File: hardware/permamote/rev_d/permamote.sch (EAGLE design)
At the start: 125 parts, among them J1 TC2030-JLINK-NL, J5 MICRO_USB_B_HIROSE_ZX62R-B-5P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, Q1 PMDXB950UPEL, Q10 PMDXB950UPEL, Q2 PMDXB950UPEL, Q3 PMDXB950UPEL, Q4 PMDXB950UPEL, Q5 PMDXB950UPEL, Q6 PMDXB950UPEL, Q7 PMDXB950UPEL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

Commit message: Fix exti in rev d
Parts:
- removed C21: 0.1uF, passives:CAPACITOR0402_CAP
- removed J5: MICRO_USB_B_HIROSE_ZX62R-B-5P(30), connector:MICRO_USB_B_HIROSE_ZX62R-B-5P(30)
- removed SJ2, SJ3, SJ4, SJ5: SOLDERJUMPERNC2, SparkFun-Passives:SOLDERJUMPERNC2
- removed U4: FT232RQ, ftdichip:FT232RQ
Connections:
- removed net !FTDI_RESET: SJ3.2, U4.!RESET
- removed net D+: J5.D+, U4.USBDP
- removed net D-: J5.D-, U4.USBDM
- removed net FTDI_VCCIO: SJ2.2, U4.VCCIO
- removed net N$13: C21.1, U4.3V3OUT
- removed net RXD: SJ4.1, U4.RXD
- removed net TXD: SJ5.1, U4.TXD
- removed net USB_5V: J5.+5V, U4.VCC
- net !RST: no longer SJ3.1
- net DBG_RX: no longer SJ5.2
- net DBG_TX: no longer SJ4.2
- net GND: now also U1.EXTI; no longer C21.2, J5.GND, U4.GND, U4.GND@1, U4.GND@2, U4.GND@A, U4.TEST
- net VCC: no longer SJ2.1

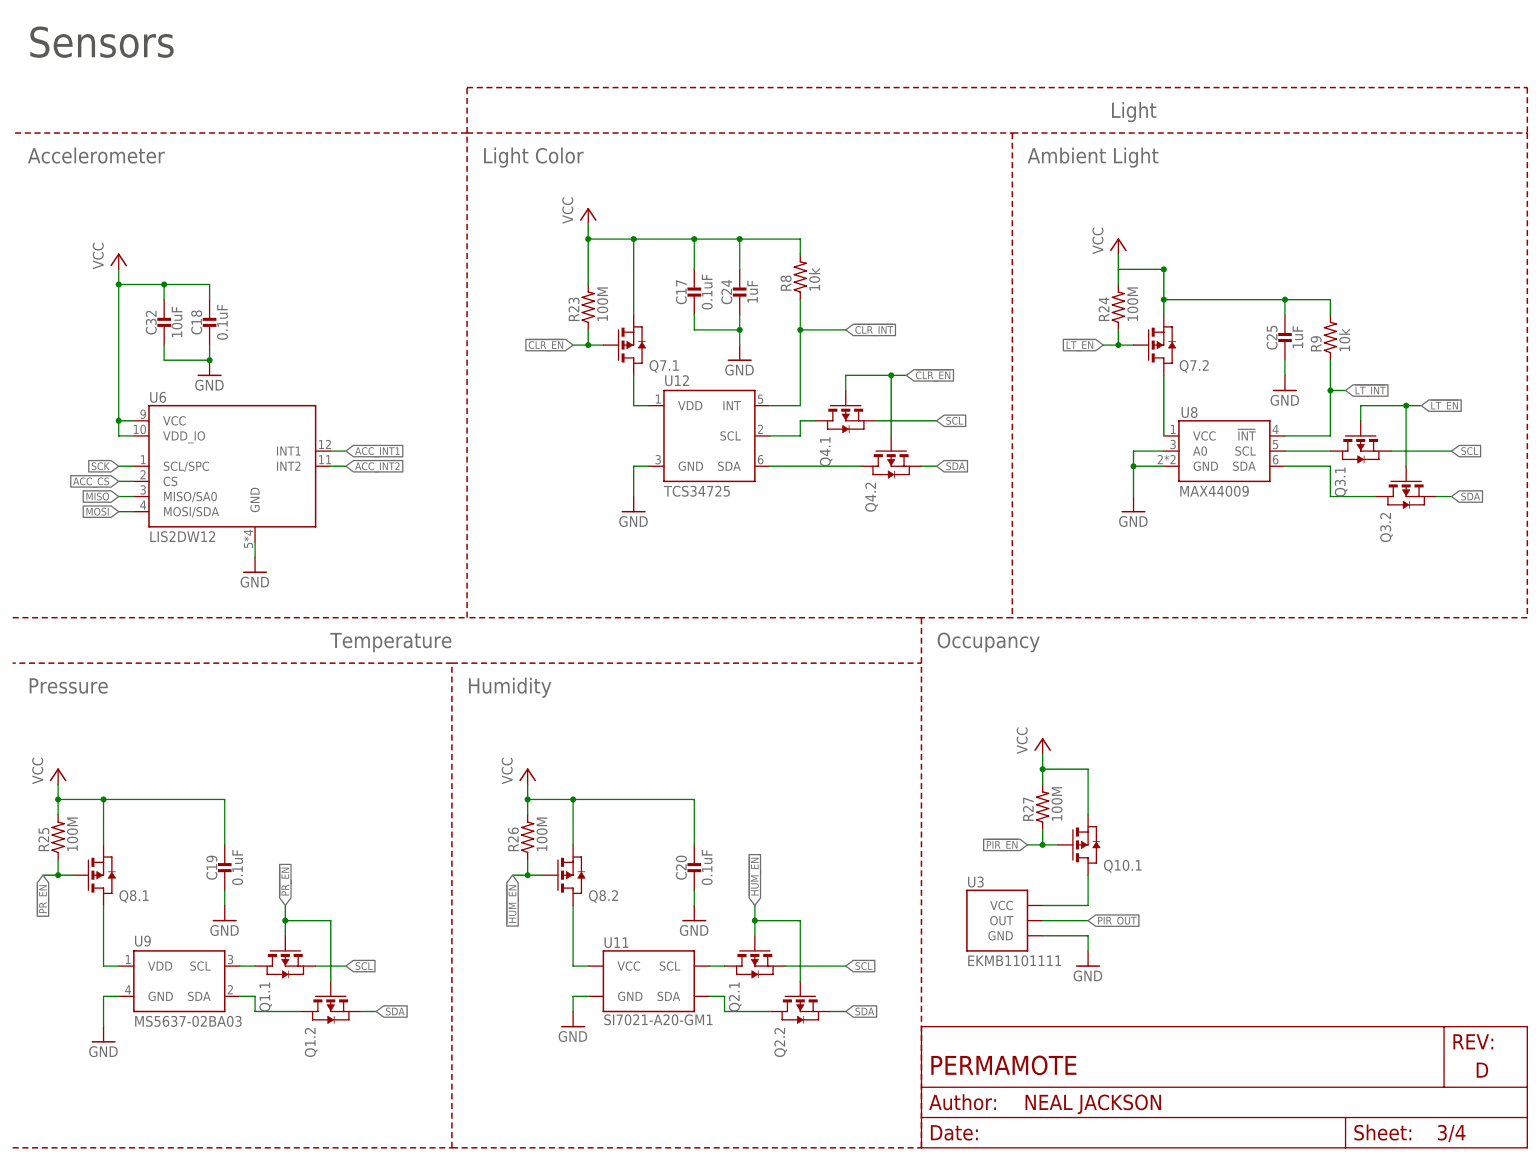
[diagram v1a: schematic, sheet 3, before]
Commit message: switch to larger coin cell, new light sensor
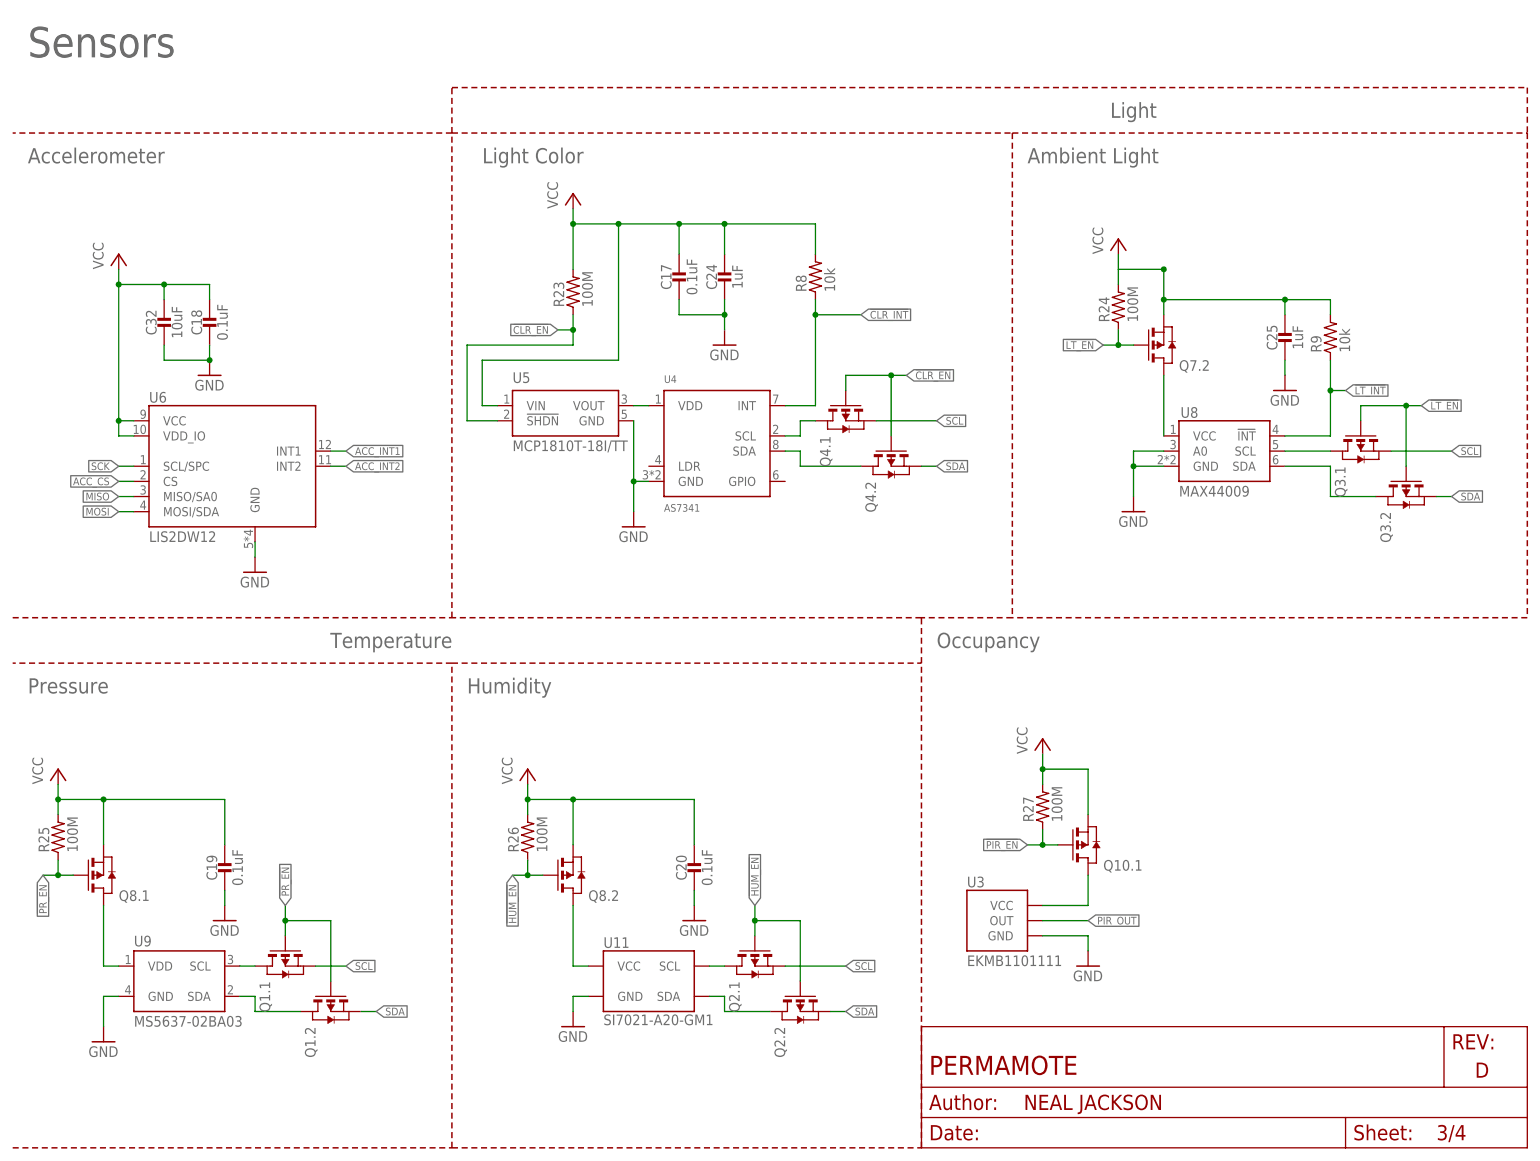
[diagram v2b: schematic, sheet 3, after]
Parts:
- removed BT2, BT3: BAT-HLD-002-THM, batteries:BAT-HLD-002-THM
- removed BT4: BAT_PACKCR123A, batteries:BAT_PACKCR123A
- removed U12: TCS34725, chips:TCS34725
- added BAT1: 2477THMCOINCELLCLIP, batteries:2477THMCOINCELLCLIP
- added U4: AS7341, chips:AS7341
- added U5: MCP1810T-18I/TT, chips:MCP1810T-18I/TT
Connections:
- removed net N$54: Q4.2.D, U12.SDA
- new net N$13: Q4.2.D, U4.SDA
- net !CLR_EN: now also U5.!SHDN; no longer Q7.1.G
- net !CLR_INT: now also U4.INT; no longer U12.INT
- net GND: now also BAT1.-, U4.GND, U5.GND; no longer BT2.-, BT3.-, BT4.-, U12.GND
- net N$31: now also U4.VDD, U5.VOUT; no longer Q7.1.D, U12.VDD
- net N$55: now also U4.SCL; no longer U12.SCL
- net VBAT: now also BAT1.+; no longer BT2.+, BT3.+, BT4.+
- net VCC: now also U5.VIN; no longer Q7.1.S
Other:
- note removed: "Note: Only populate one type of battery holder"
- moved on the sheet: C17, C24, R23, R8
